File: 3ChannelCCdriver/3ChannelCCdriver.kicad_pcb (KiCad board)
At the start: 2 copper layers, 49 x 49 mm, 55 parts, among them J1 BB10-10S-02, J2 Screw_Terminal_01x02, J3 Screw_Terminal_01x02, J4 Screw_Terminal_01x02, J5 Screw_Terminal_01x02, U1 AL8860WT-7, U2 AL8860WT-7, U3 AL8860WT-7, U4 TPS54202DDC, U5 XL6019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

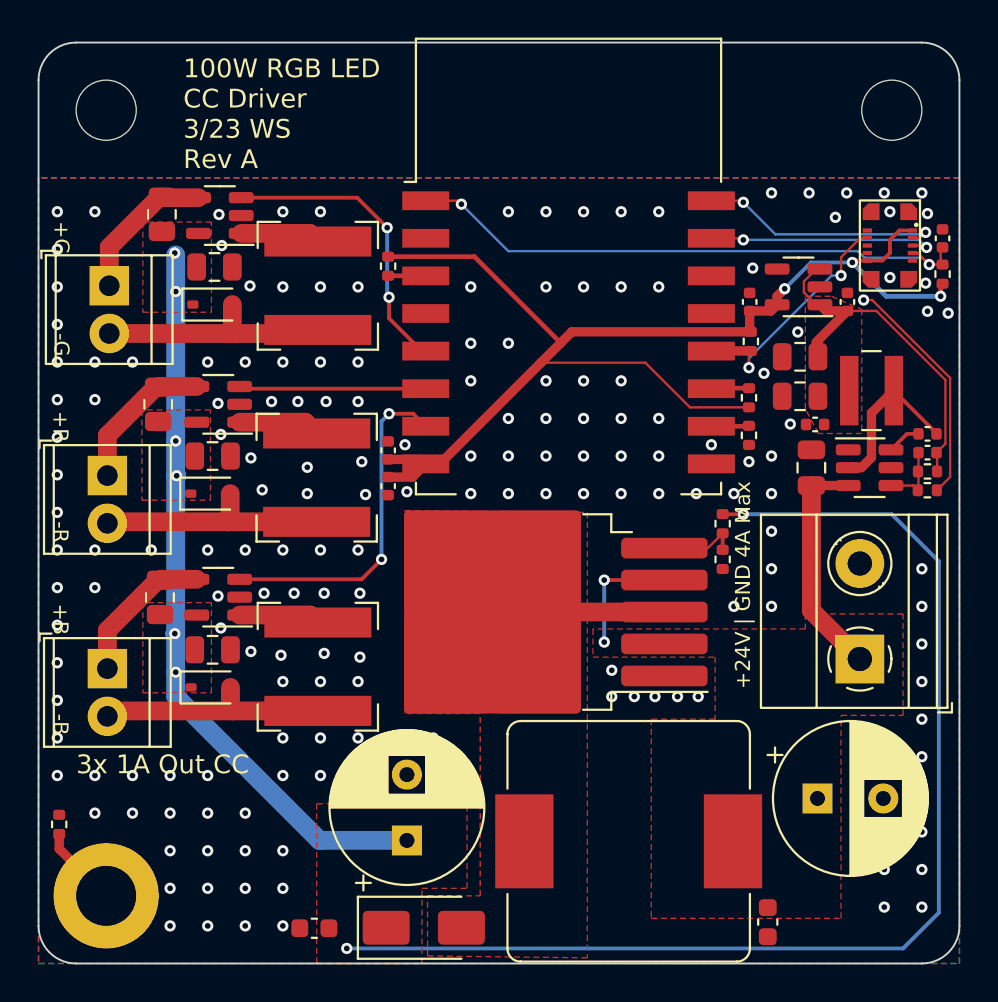
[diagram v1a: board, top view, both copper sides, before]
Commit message: Changed rev to B01
Changed diode pinout on CC driver
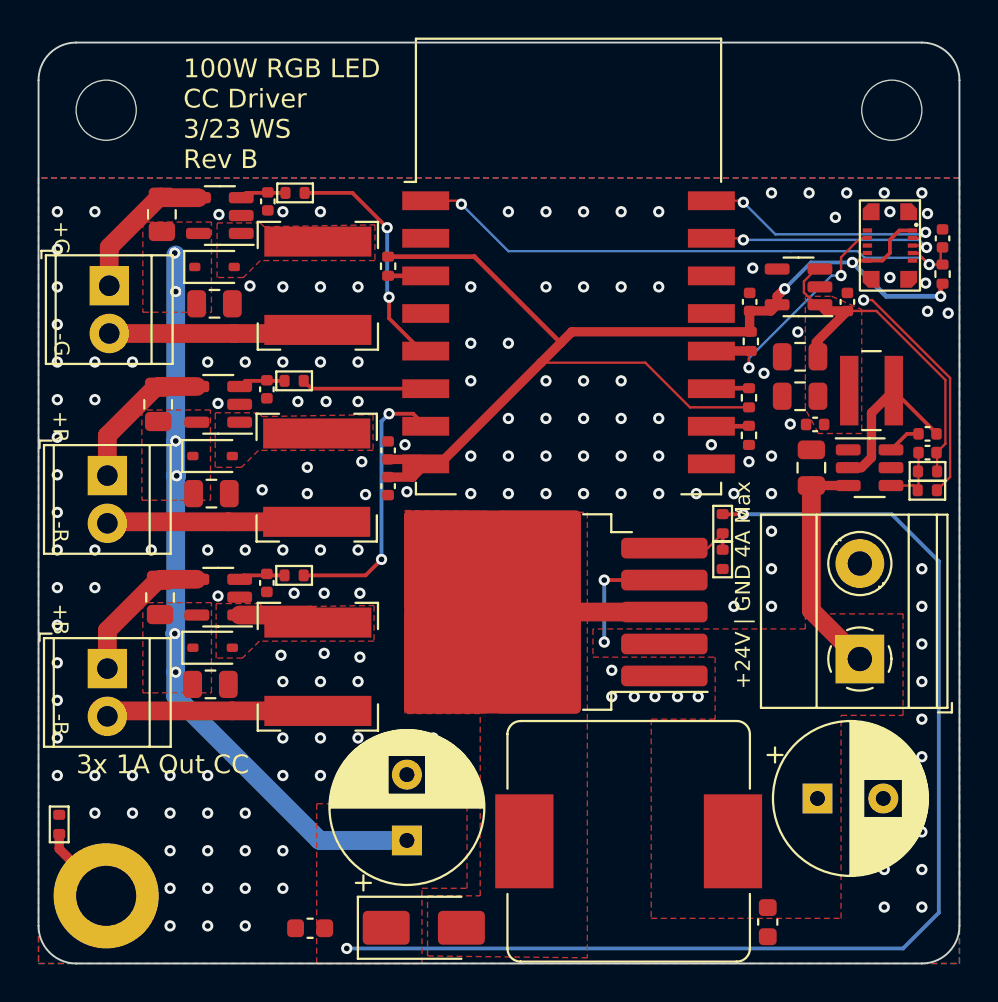
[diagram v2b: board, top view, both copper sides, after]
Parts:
- added C19: 0402,1uF,25V,X5R, Capacitor_SMD:C_0402_1005Metric, F.Cu at (90.6, 48.0)
- added C20: 0402,1uF,25V,X5R, Capacitor_SMD:C_0402_1005Metric, F.Cu at (90.5, 58.0)
- added C21: 0402,1uF,25V,X5R, Capacitor_SMD:C_0402_1005Metric, F.Cu at (90.5, 68.3)
- added R10: 0402,4.7k, PCM_Resistor_SMD_AKL:R_0402_1005Metric, F.Cu at (92.0, 57.6)
- added R11: 0402,4.7k, PCM_Resistor_SMD_AKL:R_0402_1005Metric, F.Cu at (92.0, 68.0)
- added R7: 0402,4.7k, PCM_Resistor_SMD_AKL:R_0402_1005Metric, F.Cu at (92.0, 47.6)
- R4, R5, R6, R8, R9: footprint Resistor_SMD:R_0402_1005Metric -> PCM_Resistor_SMD_AKL:R_0402_1005Metric
- moved D3 2.11 mm to (87.7, 71.8)
- moved D2 2.00 mm to (87.7, 61.6)
- moved D1 2.00 mm to (87.8, 51.5)
- moved C2 2.00 mm to (87.6, 63.6)
- moved C1 1.96 mm to (87.8, 53.5)
- moved C3 1.84 mm to (87.5, 73.8)
- moved C12 0.23 mm to (92.8, 86.7)
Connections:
- D1 pad 2: /CCDriver_1Ch3/LED- -> /CCDriver_1Ch3/SW
- D2 pad 2: /CCDriver_1Ch1/LED- -> /CCDriver_1Ch1/SW
- D3 pad 2: /CCDriver_1Ch2/LED- -> /CCDriver_1Ch2/SW
- L1 pad 1: Net-(U1-SW) -> /CCDriver_1Ch3/SW
- L2 pad 1: Net-(U2-SW) -> /CCDriver_1Ch1/SW
- L3 pad 1: Net-(U3-SW) -> /CCDriver_1Ch2/SW
- U1 pad 1: Net-(U1-SW) -> /CCDriver_1Ch3/SW
- U1 pad 3: /CCDriver_1Ch3/CTRL -> Net-(U1-CTRL)
- U2 pad 1: Net-(U2-SW) -> /CCDriver_1Ch1/SW
- U2 pad 3: /CCDriver_1Ch1/CTRL -> Net-(U2-CTRL)
- U3 pad 1: Net-(U3-SW) -> /CCDriver_1Ch2/SW
- U3 pad 3: /CCDriver_1Ch2/CTRL -> Net-(U3-CTRL)
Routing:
- net Net-(U2-SW): track 4.35 -> 0.00 mm
- net Net-(U3-SW): track 4.33 -> 0.00 mm
- net /CCDriver_1Ch2/SW: track 0.00 -> 4.33 mm
- net Net-(U1-SW): track 4.26 -> 0.00 mm
- net /CCDriver_1Ch2/CTRL: track 18.1 -> 14.6 mm
- net /CCDriver_1Ch1/CTRL: track 9.95 -> 6.66 mm
- net /CCDriver_1Ch3/CTRL: track 16.0 -> 12.7 mm
- net Net-(U2-CTRL): track 0.00 -> 2.68 mm
- net Net-(U3-CTRL): track 0.00 -> 2.48 mm
- net Net-(U1-CTRL): track 0.00 -> 2.46 mm
- net /CCDriver_1Ch3/LED-: track 12.8 -> 11.2 mm
- net /CCDriver_1Ch1/LED-: track 12.7 -> 11.2 mm
- net /CCDriver_1Ch2/LED-: track 12.6 -> 11.3 mm
- net GND: vias 177 -> 169
- added copper zone on F.Cu, net /CCDriver_1Ch1/SW
- added copper zone on F.Cu, net /CCDriver_1Ch2/SW
- added copper zone on F.Cu, net /CCDriver_1Ch3/SW
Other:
- board text added: "100W RGB LED CC Driver 3/23 WS Rev B"
- board text removed: "100W RGB LED CC Driver 3/23 WS Rev A"
